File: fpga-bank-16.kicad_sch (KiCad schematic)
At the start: 3 parts, among them U4 XC7K160T-FFG676, Y3 Oscillator_100MHz_ASFL1

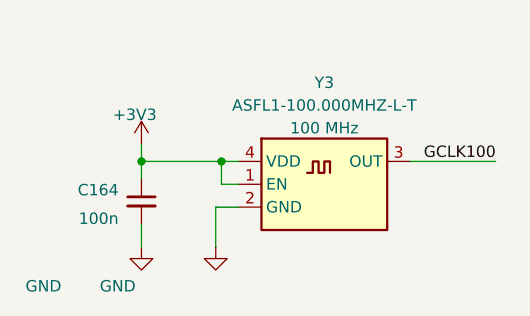
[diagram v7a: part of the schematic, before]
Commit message: Add updated components to local library
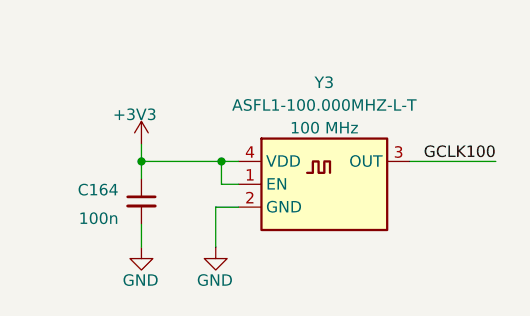
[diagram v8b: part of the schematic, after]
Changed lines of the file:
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@@
     (effects (font (size 1.27 1.27)) (justify right))
   )
-  (symbol (lib_id "power:GND") (at 34.29 267.335 0) (mirror y) (unit 1)
+  (symbol (lib_id "sodimm-ddr5-tester:GND") (at 34.29 267.335 0) (mirror y) (unit 1)
     (in_bom yes) (on_board yes) (fields_autoplaced)
     (property "Reference" "#PWR0265" (id 0) (at 34.29 273.685 0)
       (effects (font (size 1.27 1.27)) hide)
     )
-    (property "Value" "GND" (id 1) (at 25.4 272.415 0)
+    (property "Value" "GND" (id 1) (at 36.195 271.78 0)
       (effects (font (size 1.27 1.27) (thickness 0.15)) (justify left bottom))
     )
@@
       (effects (font (size 1.27 1.27) (thickness 0.15)) (justify left bottom) hide)
     )
-    (property "Author" "Antmicro" (id 4) (at 25.4 274.955 0)
-      (effects (font (size 1.27 1.27) (thickness 0.15)) (justify left bottom) hide)
-    )
-    (property "License" "Apache-2.0" (id 5) (at 25.4 277.495 0)
+    (property "Author" "Antmicro" (id 4) (at 25.4 272.415 0)
+      (effects (font (size 1.27 1.27) (thickness 0.15)) (justify left bottom) hide)
+    )
+    (property "License" "Apache-2.0" (id 5) (at 25.4 274.955 0)
       (effects (font (size 1.27 1.27) (thickness 0.15)) (justify left bottom) hide)
     )
@@
     (pin "T6")
   )
-  (symbol (lib_id "power:+3V3") (at 26.035 255.905 0) (unit 1)
+  (symbol (lib_id "sodimm-ddr5-tester:+3V3") (at 26.035 255.905 0) (unit 1)
     (in_bom yes) (on_board yes) (fields_autoplaced)
     (property "Reference" "#PWR0263" (id 0) (at 26.035 259.715 0)
@@
     (pin "1")
   )
-  (symbol (lib_id "power:GND") (at 26.035 267.335 0) (mirror y) (unit 1)
+  (symbol (lib_id "sodimm-ddr5-tester:GND") (at 26.035 267.335 0) (mirror y) (unit 1)
     (in_bom yes) (on_board yes) (fields_autoplaced)
     (property "Reference" "#PWR0264" (id 0) (at 26.035 273.685 0)
       (effects (font (size 1.27 1.27)) hide)
     )
-    (property "Value" "GND" (id 1) (at 17.145 272.415 0)
+    (property "Value" "GND" (id 1) (at 27.94 271.78 0)
       (effects (font (size 1.27 1.27) (thickness 0.15)) (justify left bottom))
     )
@@
       (effects (font (size 1.27 1.27) (thickness 0.15)) (justify left bottom) hide)
     )
-    (property "Author" "Antmicro" (id 4) (at 17.145 274.955 0)
-      (effects (font (size 1.27 1.27) (thickness 0.15)) (justify left bottom) hide)
-    )
-    (property "License" "Apache-2.0" (id 5) (at 17.145 277.495 0)
+    (property "Author" "Antmicro" (id 4) (at 17.145 272.415 0)
+      (effects (font (size 1.27 1.27) (thickness 0.15)) (justify left bottom) hide)
+    )
+    (property "License" "Apache-2.0" (id 5) (at 17.145 274.955 0)
       (effects (font (size 1.27 1.27) (thickness 0.15)) (justify left bottom) hide)
     )
     (pin "1")
   )
-  (symbol (lib_id "power:+3V3") (at 184.15 71.12 0) (unit 1)
+  (symbol (lib_id "sodimm-ddr5-tester:+3V3") (at 184.15 71.12 0) (unit 1)
     (in_bom yes) (on_board yes) (fields_autoplaced)
     (property "Reference" "#PWR0262" (id 0) (at 184.15 74.93 0)
